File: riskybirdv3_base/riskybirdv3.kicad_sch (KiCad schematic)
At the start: 180 parts, among them IC1 PMW3901MB-TXQT, J1 USB_B_Micro, J10 Conn_01x05, J11 Conn_01x05, J13 Conn_02x12_Odd_Even_MountingP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, J18 Conn_01x05_MountingPin, J19 Conn_01x30_MountingPin, J2 Conn_01x05, J3 Conn_01x02, J4 Conn_01x02, J5 Conn_01x02, J6 Conn_01x02, J7 Conn_01x02, J8 USB_B_Micro, J9 Conn_01x05, Q1 SI2302, Q2 SI2302, Q3 SI2302, Q4 SI2302, Q8 BC847BDW1, SW1 SW_SPST, SW2 SW_SPST, SW3 SW_SPST, SW4 SW_SPST, U1 ADS7128IRTER, U10 TLV70018DCKR, U11 TPS54331D, U12 LP2985-3.0, U13 TPS2113A, U14 ESP32-C6-MINI-1/U, U3 BMI088, U4 MCP73831-2-OT, U6 FT2232HL-REEL, U7 TPS2113A, U8 FT231XS, U9 VL53L1CXV0FY1, Y1 f

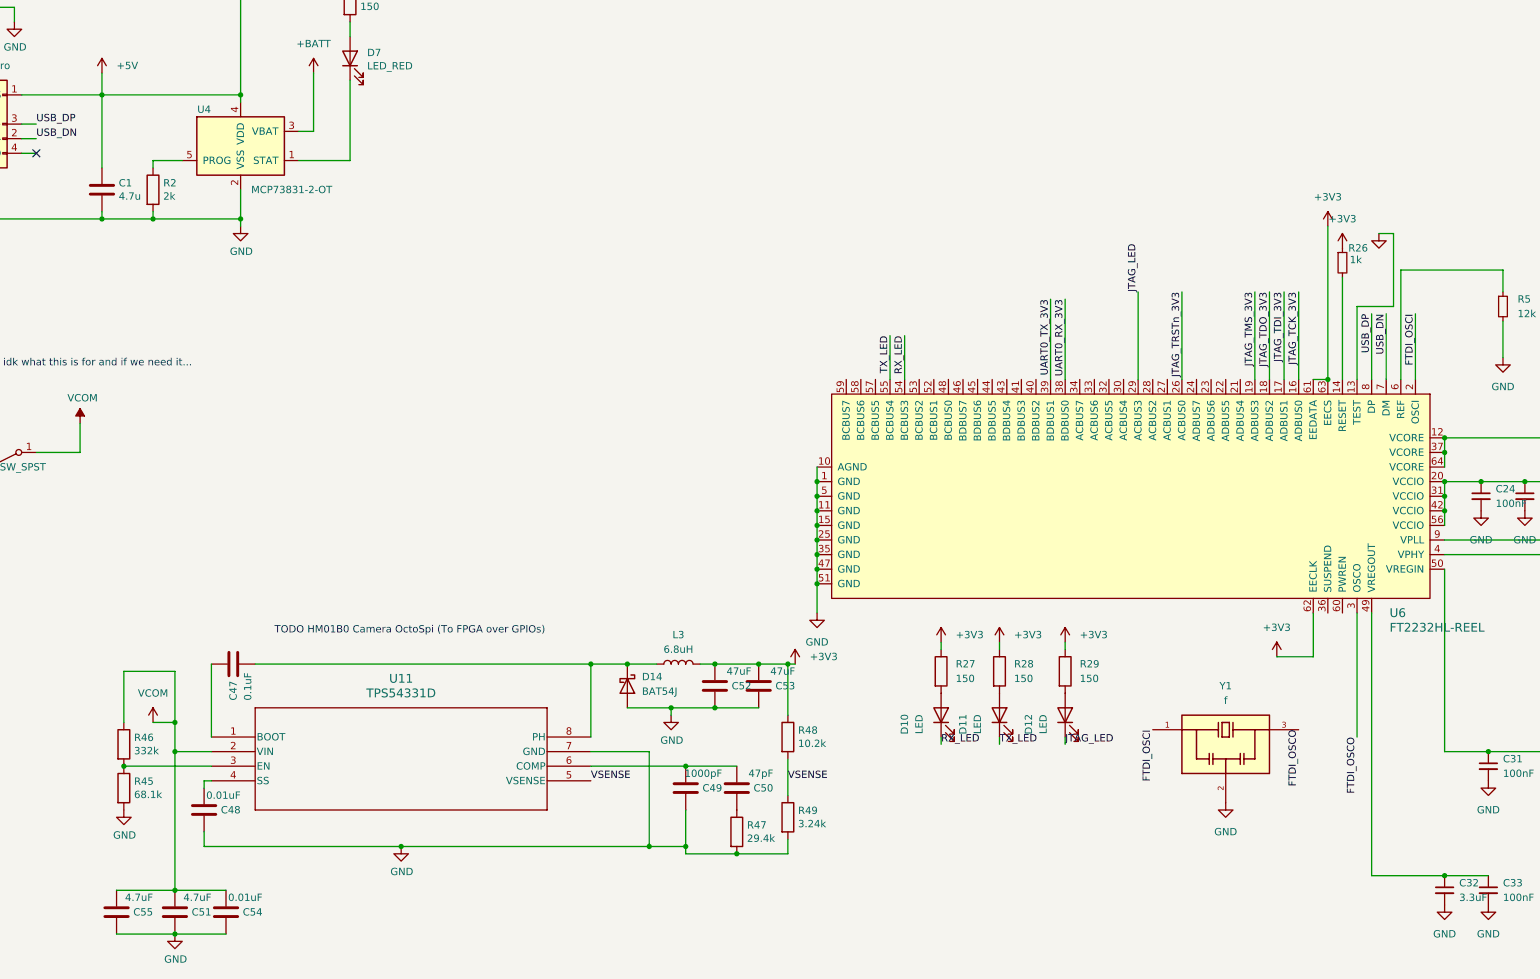
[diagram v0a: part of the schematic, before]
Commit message: riskybirdv3: add LTC3119 buck-boost (U2) + LCSC library
- Place LTC3119EUFD#TRPBF (U2) in the schematic and configure it:
  RT R62=48.7k (1.5MHz), L4=2.2uH, FB R59/R60 316k/100k -> 3.31V,
  bootstrap C60/C61, PWM/SYNC=GND (Burst).
- Import LTC3119 symbol/footprint/3D as riskybird_lcsc library
  (LCSC C580693); register lib in sym-lib-table.
- Include the referenced project symbol libs (2025-12-16, FX23L) and
  the 5037762410 (Molex 2x12) footprint so the tables aren't dangling.

Note: fp-lib-table still needs a riskybird_lcsc entry to resolve the
LTC3119 footprint; RUN-pin UVLO divider not yet built.
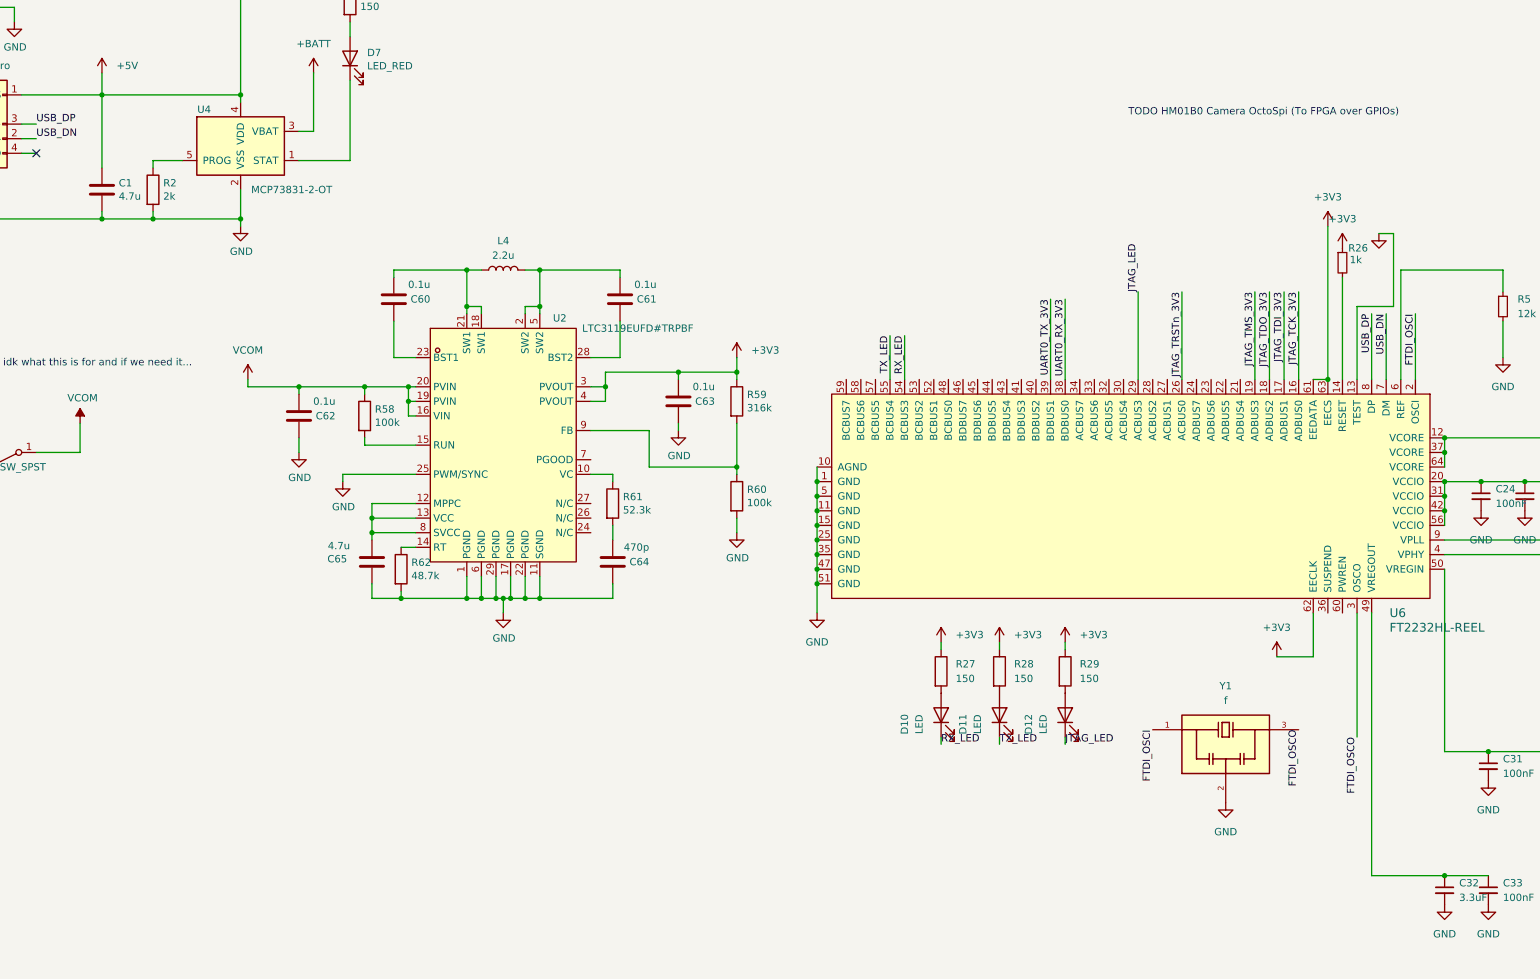
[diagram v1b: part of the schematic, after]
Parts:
- removed C47: 0.1uF, Capacitor_SMD:C_0201_0603Metric, symbol Device:C
- removed C48, C54: 0.01uF, Capacitor_SMD:C_0201_0603Metric, symbol Device:C
- removed C49: 1000pF, Capacitor_SMD:C_0201_0603Metric, symbol Device:C
- removed C50: 47pF, Capacitor_SMD:C_0201_0603Metric, symbol Device:C
- removed C51, C55: 4.7uF, Capacitor_SMD:C_0201_0603Metric, symbol Device:C
- removed C52, C53: 47uF, Capacitor_SMD:C_0603_1608Metric_Pad1.08x0.95mm_HandSolder, symbol Device:C
- removed D14: BAT54J, Diode_SMD:D_SOD-323F, symbol Diode:BAT54J
- removed L3: 6.8uH, Inductor_SMD:L_0603_1608Metric, symbol Device:L
- removed R45: 68.1k, Resistor_SMD:R_0201_0603Metric, symbol Device:R
- removed R46: 332k, Resistor_SMD:R_0201_0603Metric, symbol Device:R
- removed R47: 29.4k, Resistor_SMD:R_0201_0603Metric, symbol Device:R
- removed R48: 10.2k, Resistor_SMD:R_0201_0603Metric, symbol Device:R
- removed R49: 3.24k, Resistor_SMD:R_0201_0603Metric, symbol Device:R
- removed U11: TPS54331D, Package_SO:SOIC-8-1EP_3.9x4.9mm_P1.27mm_EP2.41x3.81mm, symbol 2025-12-10_10-51-20:TPS54331D
- added C60, C61: 0.1u, Capacitor_SMD:C_0201_0603Metric, symbol Device:C
- added C62: 0.1u, Capacitor_SMD:C_01005_0402Metric, symbol Device:C
- added C63: 0.1u, Capacitor_SMD:C_1206_3216Metric, symbol Device:C
- added C64: 470p, 470p, symbol Device:C
- added C65: 4.7u, Capacitor_SMD:C_0201_0603Metric, symbol Device:C
- added L4: 2.2u, Inductor_SMD:L_0603_1608Metric, symbol Device:L
- added R58, R60: 100k, Resistor_SMD:R_0201_0603Metric, symbol Device:R
- added R59: 316k, Resistor_SMD:R_0201_0603Metric, symbol Device:R
- added R61: 52.3k, Resistor_SMD:R_0201_0603Metric, symbol Device:R
- added R62: 48.7k, Resistor_SMD:R_0201_0603Metric, symbol Device:R
- added U2: LTC3119EUFD#TRPBF, riskybird_lcsc:QFN-28_L5.0-W4.0-P0.50-TL-EP, symbol riskybird_lcsc:LTC3119EUFD#TRPBF
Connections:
- net +3V3: now also C63.2, R59.1, U2.3 (PVOUT), U2.4 (PVOUT)
- net GND: now also C62.1, C63.1, C64.1, C65.1, R60.2, R62.2, U2.1 (PGND), U2.11 (SGND), U2.17 (PGND), U2.22 (PGND), U2.25 (PWM/SYNC), U2.29 (PGND), U2.6 (PGND)
- net VCOM: now also C62.2, R58.1, U2.16 (VIN), U2.19 (PVIN), U2.20 (PVIN)
- new net: R61.1, U2.10 (VC)
- new net: C65.2, U2.12 (MPPC), U2.13 (VCC), U2.8 (SVCC)
- new net: R62.1, U2.14 (RT)
- new net: R58.2, U2.15 (RUN)
- new net: C60.2, L4.1, U2.18 (SW1), U2.21 (SW1)
- new net: C61.2, L4.2, U2.2 (SW2), U2.5 (SW2)
- new net: C60.1, U2.23 (BST1)
- new net: C61.1, U2.28 (BST2)
- new net: R59.2, R60.1, U2.9 (FB)
- new net: C64.2, R61.2

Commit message: add: B2Bs, FTDIs, and off-board connectors
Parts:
- removed C18, C19, C20, C21, C22, C24, C25, C27, C29, C31, C33: 100nF, Capacitor_SMD:C_0201_0603Metric, symbol Device:C_Small
- removed C23: 10uF, Capacitor_SMD:C_0201_0603Metric, symbol Device:C_Small
- removed C28, C30: 4.7uF, Capacitor_SMD:C_0201_0603Metric, symbol Device:C_Small
- removed C32: 3.3uF, Capacitor_SMD:C_0201_0603Metric, symbol Device:C_Small
- removed D10, D11, D12: LED, LED_SMD:LED_0402_1005Metric, symbol Device:LED
- removed FB1, FB2: 600R@100MHz/0.5A, Inductor_SMD:L_0603_1608Metric, symbol Device:FerriteBead
- removed J10, J11, J2, J9: Conn_01x05, Connector_PinHeader_2.54mm:PinHeader_1x05_P2.54mm_Vertical, symbol Connector_Generic:Conn_01x05
- removed R26: 1k, Resistor_SMD:R_0201_0603Metric, symbol Device:R_Small
- removed R27, R28, R29: 150, Resistor_SMD:R_0201_0603Metric, symbol Device:R
- removed R41, R42: 10k, Resistor_SMD:R_0201_0603Metric, symbol Device:R_Small
- removed R43, R44: 4.7K, Resistor_SMD:R_0201_0603Metric, symbol Device:R_Small
- removed R5: 12k, Resistor_SMD:R_0201_0603Metric, symbol Device:R_Small
- removed U6: FT2232HL-REEL, Package_QFP:LQFP-64_10x10mm_P0.5mm, symbol dk_Interface-Controllers:FT2232HL-REEL
- removed U9: VL53L1CXV0FY1, Sensor_Distance:ST_VL53L1x, symbol Sensor_Distance:VL53L1CXV0FY1
- removed Y1: f, riskybird:OSC_CSTNE12M0G550000R0, symbol CSTNE12M0G550000R0:CSTNE12M0G550000R0
- added C47, C49, C52, C53, C54, C55, C66, C67, C69, C71, C72, C73, C74, C75, C76, C77, C78: 100nF, Capacitor_SMD:C_0201_0603Metric, symbol Device:C_Small
- added C48: 4.7uF, Capacitor_SMD:C_0201_0603Metric, symbol Device:C_Small
- added C50, C51: 3u3, Capacitor_SMD:C_0201_0603Metric, symbol Device:C_Small
- added C68, C70: 10u, Capacitor_SMD:C_0201_0603Metric, symbol Device:C_Small
- added D14, D15, D16, D17, D18, D19: LED, LED_SMD:LED_0402_1005Metric, symbol Device:LED
- added J12, J14, J15, J16: Conn_01x05, Connector_PinHeader_2.54mm:PinHeader_1x05_P2.54mm_Vertical, symbol Connector_Generic:Conn_01x05
- added J17: Conn_02x12_Odd_Even_MountingPin, riskybird:5037762410, symbol Connector_Generic_MountingPin:Conn_02x12_Odd_Even_MountingPin
- added R41, R42, R43, R44, R49, R63: 150, Resistor_SMD:R_0201_0603Metric, symbol Device:R
- added R45, R48: 10k, Resistor_SMD:R_0201_0603Metric, symbol Device:R_Small
- added R46, R47: 4.7K, Resistor_SMD:R_0201_0603Metric, symbol Device:R_Small
- added R64, R65: 12k, symbol Device:R_Small
- added R66, R67: 1k, symbol Device:R_Small
- added U11: VL53L1CXV0FY1, Sensor_Distance:ST_VL53L1x, symbol Sensor_Distance:VL53L1CXV0FY1
- added U15, U9: FT2232HL-REEL, Package_QFP:LQFP-64_10x10mm_P0.5mm, symbol dk_Interface-Controllers:FT2232HL-REEL
- added Y2, Y3: f, riskybird:OSC_CSTNE12M0G550000R0, symbol CSTNE12M0G550000R0:CSTNE12M0G550000R0
- C39: value 4.7uF -> 100nF
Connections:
- net +3V3: now also JB1.14 (Pin_14), JB1.16 (Pin_16), C47.1, C48.1, J12.1 (Pin_1), J14.1 (Pin_1), J15.1 (Pin_1), J16.1 (Pin_1), R41.1, R42.1, R43.1, R44.1, R45.1, R46.1, R47.1, R48.1, R49.1, R63.1, U11.1 (AVDDVCSEL), U11.11 (AVDD); no longer C38.1, C39.1
- net +5V: now also JB1.2 (Pin_2), JB1.4 (Pin_4), JB1.6 (Pin_6), JB2.1 (Pin_1), JB2.3 (Pin_3), JB2.5 (Pin_5), JB2.7 (Pin_7)
- net ACCEL_INT: now also JB1.46 (Pin_46)
- net CamRST: now also JB2.71 (Pin_71)
- net GND: now also J13.MP (MountPin), J18.MP (MountPin), JB1.1 (Pin_1), JB1.13 (Pin_13), JB1.19 (Pin_19), JB1.25 (Pin_25), JB1.30 (Pin_30), JB1.33 (Pin_33), JB1.43 (Pin_43), JB1.53 (Pin_53), JB1.54 (Pin_54), JB1.63 (Pin_63), JB1.64 (Pin_64), JB1.7 (Pin_7), JB1.73 (Pin_73), JB1.74 (Pin_74), JB1.83 (Pin_63), JB1.89 (Pin_69), JB1.SH (Shield), JB2.19 (Pin_19), JB2.29 (Pin_29), JB2.30 (Pin_30), JB2.39 (Pin_39), JB2.40 (Pin_40), JB2.49 (Pin_49), JB2.50 (Pin_50), JB2.59 (Pin_59), JB2.60 (Pin_60), JB2.69 (Pin_69), JB2.70 (Pin_70), JB2.79 (Pin_79), JB2.80 (Pin_80), JB2.89 (Pin_69), JB2.SH (Shield), JB3.11 (Pin_11), JB3.12 (Pin_12), JB3.17 (Pin_17), JB3.18 (Pin_18), JB3.23 (Pin_23), JB3.24 (Pin_24), JB3.29 (Pin_29), JB3.30 (Pin_30), JB3.35 (Pin_35), JB3.36 (Pin_36), JB3.45 (Pin_45), JB3.46 (Pin_46), JB3.5 (Pin_5), JB3.55 (Pin_55), JB3.6 (Pin_6), JB3.SH (Shield), C47.2, C48.2, C49.2, C50.2, C51.2, C52.2, C53.2, C54.2, C55.2, C66.2, C67.2, C68.2, C69.2, C70.2, C71.2, C72.2, C73.2, C74.2, C75.2, C76.2, C77.2, C78.2, J12.2 (Pin_2), J14.2 (Pin_2), J15.2 (Pin_2), J16.2 (Pin_2), J17.MP (MountPin), R64.2, R65.2, U11.12 (GND), U11.2 (AVSSVCSEL), U11.3 (GND), U11.4 (GND), U11.6 (GND), U15.1 (GND), U15.10 (AGND), U15.11 (GND), U15.13 (TEST), U15.15 (GND), U15.25 (GND), U15.35 (GND), U15.47 (GND), U15.5 (GND), U15.51 (GND), U9.1 (GND), U9.10 (AGND), U9.11 (GND), U9.13 (TEST), U9.15 (GND), U9.25 (GND), U9.35 (GND), U9.47 (GND), U9.5 (GND), U9.51 (GND), Y2.2, Y3.2
- net GPIO1: now also J12.5 (Pin_5)
- net GPIO2: now also J15.5 (Pin_5)
- net GPIO3: now also J14.5 (Pin_5)
- net GPIO4: now also J16.5 (Pin_5)
- net GYRO_INT: now also JB1.48 (Pin_48)
- net INT_BARO: now also JB1.52 (Pin_52)
- net LED_N: now also JB2.75 (Pin_75)
- net MISO: now also JB2.63 (Pin_63)
- net MOSI: now also JB2.65 (Pin_65)
- net MOTION: now also JB2.73 (Pin_73)
- net MOTOR1: now also JB1.32 (Pin_32)
- net MOTOR2: now also JB1.35 (Pin_35)
- net MOTOR3: now also JB1.100 (Pin_80)
- net MOTOR4: now also JB1.99 (Pin_79)
- net NCS: now also JB2.67 (Pin_67)
- net SCL: now also J13.8 (Pin_8), JB2.23 (Pin_23), J12.3 (Pin_3), J14.3 (Pin_3), J15.3 (Pin_3), J16.3 (Pin_3), R46.2, U11.10 (SCL)
- net SCLK: now also JB2.61 (Pin_61)
- net SDA: now also J13.7 (Pin_7), JB2.21 (Pin_21), J12.4 (Pin_4), J14.4 (Pin_4), J15.4 (Pin_4), J16.4 (Pin_4), R47.2, U11.9 (SDA)
- net TOF_Int: now also JB1.50 (Pin_50), R48.2, U11.7 (GPIO1)
- net VIOTB: now reaches JB2.10 (Pin_10)
- net VIOTB: now also JB1.10 (Pin_10), JB1.12 (Pin_12), JB2.2 (Pin_2), JB2.4 (Pin_4), JB2.6 (Pin_6), JB2.8 (Pin_8)
- net TCK_2: now reaches JB2.100 (Pin_80)
- net TCK_2: now also J17.2 (Pin_2), U15.16 (ADBUS0)
- net 3v3OUT: now reaches JB2.11 (Pin_11)
- net 3v3OUT: now also JB2.9 (Pin_9)
- net TRIG: now reaches JB2.25 (Pin_25)
- net TRIG: now also J13.3 (Pin_3)
- net INT: now reaches JB2.27 (Pin_27)
- net INT: now also J13.10 (Pin_10)
- net FLVD: now reaches JB2.31 (Pin_31)
- net FLVD: now also J13.6 (Pin_6)
- net MCLK: now reaches JB2.33 (Pin_33)
- net MCLK: now also J13.13 (Pin_13)
- net LVLD: now reaches JB2.35 (Pin_35)
- net LVLD: now also J13.5 (Pin_5)
- net PCLK: now reaches JB2.37 (Pin_37)
- net PCLK: now also J13.15 (Pin_15)
- net D0: now reaches JB2.41 (Pin_41)
- net D0: now also J13.18 (Pin_18)
- net D1: now reaches JB2.43 (Pin_43)
- net D1: now also J13.17 (Pin_17)
- net D2: now reaches JB2.45 (Pin_45)
- net D2: now also J13.20 (Pin_20)
- net D3: now reaches JB2.47 (Pin_47)
- net D3: now also J13.19 (Pin_19)
- net D4: now reaches JB2.51 (Pin_51)
- net D4: now also J13.22 (Pin_22)
- net D5: now reaches JB2.53 (Pin_53)
- net D5: now also J13.21 (Pin_21)
- net D6: now reaches JB2.55 (Pin_55)
- net D6: now also J13.24 (Pin_24)
- net D7: now reaches JB2.57 (Pin_57)
- net D7: now also J13.23 (Pin_23)
- net FTDI_3v3_2: now reaches JB2.92 (Pin_72)
- net FTDI_3v3_2: now also C70.1, C71.1, C72.1, C73.1, C74.1, C76.1, C78.1, R67.1, U15.14 (RESET), U15.20 (VCCIO), U15.31 (VCCIO), U15.4 (VPHY), U15.42 (VCCIO), U15.50 (VREGIN), U15.56 (VCCIO), U15.61 (EEDATA), U15.62 (EECLK), U15.63 (EECS)
- net TMS_2: now reaches JB2.94 (Pin_74)
- net TMS_2: now also J17.8 (Pin_8), U15.19 (ADBUS3)
- net TDI_2: now reaches JB2.96 (Pin_76)
- net TDI_2: now also J17.4 (Pin_4), U15.17 (ADBUS1)
- net TDO_2: now reaches JB2.98 (Pin_78)
- net TDO_2: now also J17.6 (Pin_6), U15.18 (ADBUS2)
- net AVDD: now reaches J13.1 (Pin_1)
- net DVDD: now reaches J13.11 (Pin_11)
- net IOVDD: now reaches J13.12 (Pin_12)
- net DGND: now reaches J13.14 (Pin_14)
- net DGND: now also J13.16 (Pin_16), J13.4 (Pin_4), J13.9 (Pin_9)
- net AGND: now reaches J13.2 (Pin_2)
- net Some_Top_Reset: now reaches JB1.34 (Pin_34)
- net VIDB (1.8V ?): now reaches JB1.40 (Pin_40)
- net RXD_1: now reaches JB1.42 (Pin_42)
- net RXD_1: now also J17.13 (Pin_13), U9.39 (BDBUS1)
- net TXD_1: now reaches JB1.44 (Pin_44)
- net TXD_1: now also J17.15 (Pin_15), U9.38 (BDBUS0)
- net TCK_1: now reaches JB1.45 (Pin_45)
- net TCK_1: now also J17.1 (Pin_1), U9.16 (ADBUS0)
- net TDI_1: now reaches JB1.47 (Pin_47)
- net TDI_1: now also J17.3 (Pin_3), U9.17 (ADBUS1)
- net TDO_1: now reaches JB1.49 (Pin_49)
- net TDO_1: now also J17.5 (Pin_5), U9.18 (ADBUS2)
- net TMS_1: now reaches JB1.51 (Pin_51)
- net TMS_1: now also J17.7 (Pin_7), U9.19 (ADBUS3)
- net VBAT: now reaches JB1.80 (Pin_80)
- net TXD_2: now reaches JB1.86 (Pin_66)
- net TXD_2: now also J17.16 (Pin_16), U15.38 (BDBUS0)
- net RXD_2: now reaches JB1.91 (Pin_71)
- net RXD_2: now also J17.14 (Pin_14), U15.39 (BDBUS1)
- new net: D17.2 (A), R44.2
- new net: D14.2 (A), R41.2
- new net: D16.2 (A), R43.2
- new net: D18.2 (A), R49.2
- new net: R65.1, U15.6 (REF)
- new net: C38.1, C39.1, C49.1, C50.1, U15.12 (VCORE), U15.37 (VCORE), U15.49 (VREGOUT), U15.64 (VCORE)
- new net: R67.2, U15.9 (VPLL)
- new net: C51.1, C52.1, C53.1, C54.1, U9.12 (VCORE), U9.37 (VCORE), U9.49 (VREGOUT), U9.64 (VCORE)
- new net: R64.1, U9.6 (REF)
- new net: R66.2, U9.9 (VPLL)
- new net: R45.2, U11.5 (XSHUT)
- new net: D19.2 (A), R63.2
- new net: D15.2 (A), R42.2
- new net FTDI_3v3_1: C55.1, C66.1, C67.1, C68.1, C69.1, C75.1, C77.1, R66.1, U9.14 (RESET), U9.20 (VCCIO), U9.31 (VCCIO), U9.4 (VPHY), U9.42 (VCCIO), U9.50 (VREGIN), U9.56 (VCCIO), U9.61 (EEDATA), U9.62 (EECLK), U9.63 (EECS)
- new net FTDI_OSCI_1: U9.2 (OSCI), Y3.1
- new net FTDI_OSCI_2: U15.2 (OSCI), Y2.1
- new net FTDI_OSCO_1: U9.3 (OSCO), Y3.3
- new net FTDI_OSCO_2: U15.3 (OSCO), Y2.3
- new net JTAG_LED1: D19.1 (K), U9.29 (ACBUS3)
- new net JTAG_LED2: D16.1 (K), U15.29 (ACBUS3)
- new net NSRST_1: J17.9 (Pin_9), U9.27 (ACBUS1)
- new net NSRST_2: J17.10 (Pin_10), U15.27 (ACBUS1)
- new net NTRST_1: J17.11 (Pin_11), U9.26 (ACBUS0)
- new net NTRST_2: J17.12 (Pin_12), U15.26 (ACBUS0)
- new net RX_LED1: D17.1 (K), U9.54 (BCBUS3)
- new net RX_LED2: D14.1 (K), U15.54 (BCBUS3)
- new net TX_LED1: D18.1 (K), U9.55 (BCBUS4)
- new net TX_LED2: D15.1 (K), U15.55 (BCBUS4)
- new net USB_DM_2: U15.7 (DM)
- new net USB_DP_1: U9.8 (DP)
- new net USB_DP_2: U15.8 (DP)
- new net USP_DM_1: U9.7 (DM)
- no-connect marks 16 -> 233
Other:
- note added: "Barometer"
- note added: "Bitstream FTDI (2)"
- note added: "Connector to HM01B0 Camera OctoSpi Odd / Even Swapped from datasheet. Ex: datasheet 1 = 2 here"
- note added: "Connector to Programming Board"
- note added: "ELF FTDI (1)"
- note added: "I2C Expander"
- note added: "Left B2B - HR Banks, 3v3 Capable"
- note added: "Motors"
- note added: "Optical Flow Sensor"
- note added: "Programming Board (FTDIs, USBs, Charging, etc.)"
- note added: "Right and Top B2Bs - HP Banks, 1v8 Only"
- note added: "SOME TOP RESET"
- note removed: "Power B2B"
- note removed: "Signal B2B"
- note removed: "TODO HM01B0 Camera OctoSpi (To FPGA over GPIOs)"
- note removed: "a"
- note removed: "idk what this is for and if we need it..."
- moved on the sheet: C1, C2, C26, C3, C34, C35, C36, C37, C40, C41, C42, C43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

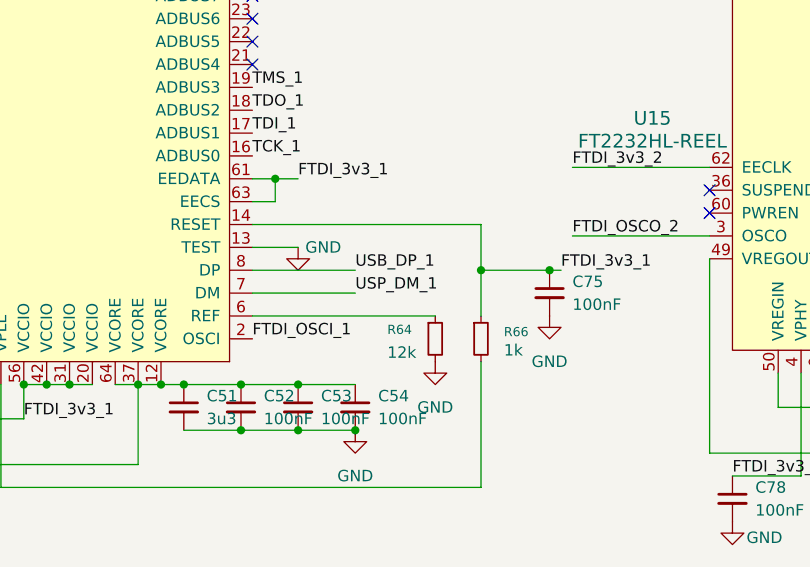
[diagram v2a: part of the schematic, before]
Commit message: add: net label typo
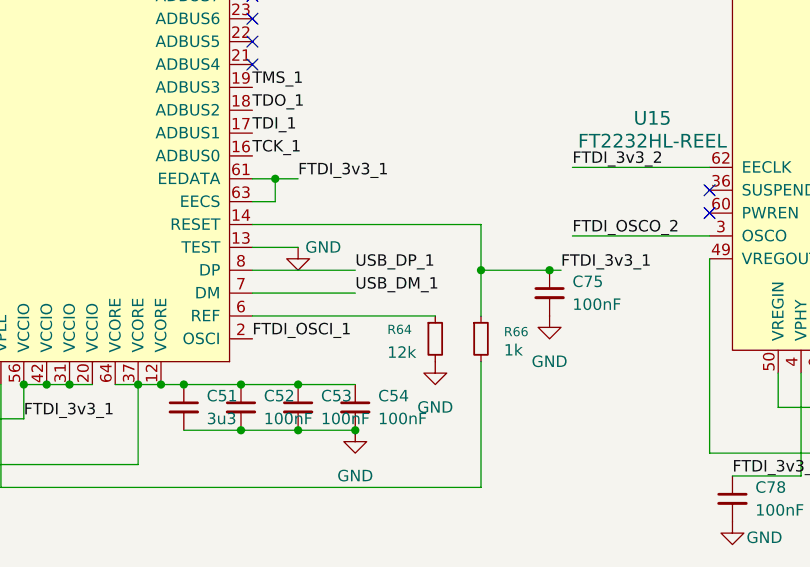
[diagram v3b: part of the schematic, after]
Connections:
- net USP_DM_1 renamed USB_DM_1
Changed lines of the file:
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@@
 		)
 	)
-	(label "USP_DM_1"
+	(label "USB_DM_1"
 		(at 725.17 129.54 0)
 		(effects
